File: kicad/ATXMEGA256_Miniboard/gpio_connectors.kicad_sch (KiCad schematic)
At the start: 6 parts, among them J10 2x5 Goldpin Socket, J11 2x5 Goldpin Socket, J12 2x3 Goldpin Socket, J13 2x5 Goldpin Socket, J14 2x5 Goldpin Socket, J9 2x5 Goldpin Socket

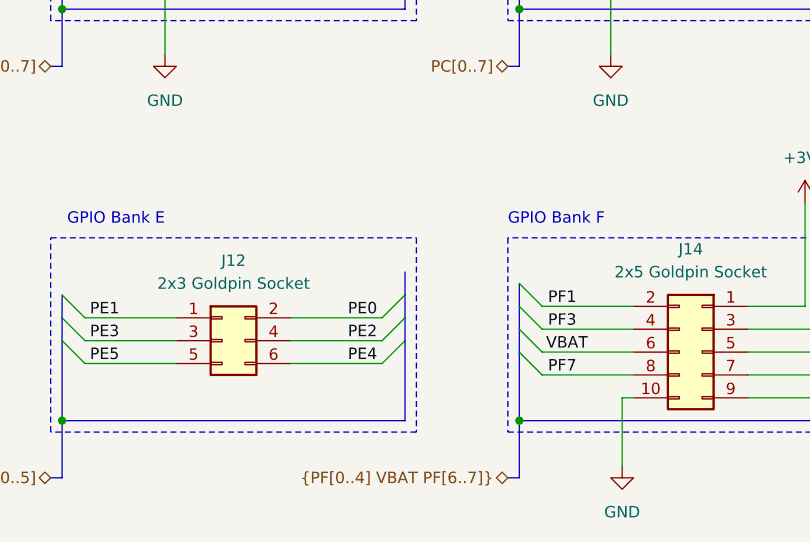
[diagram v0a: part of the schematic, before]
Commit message: Poprawiony schemat + sprawdzić czy nie są potrzebne kondensatory przy oscylatorze
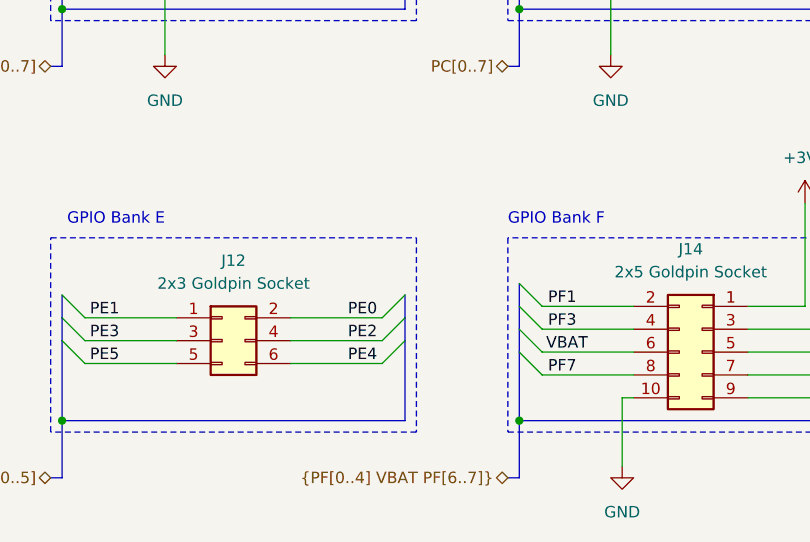
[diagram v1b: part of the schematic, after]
